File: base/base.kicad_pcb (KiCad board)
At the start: 2 copper layers, 51.4 x 20.5 mm, 12 parts, among them J1 Game Boy, J2 Game Gear, J3 Programming, U1 HC139, U2 PIC10F200-IOT

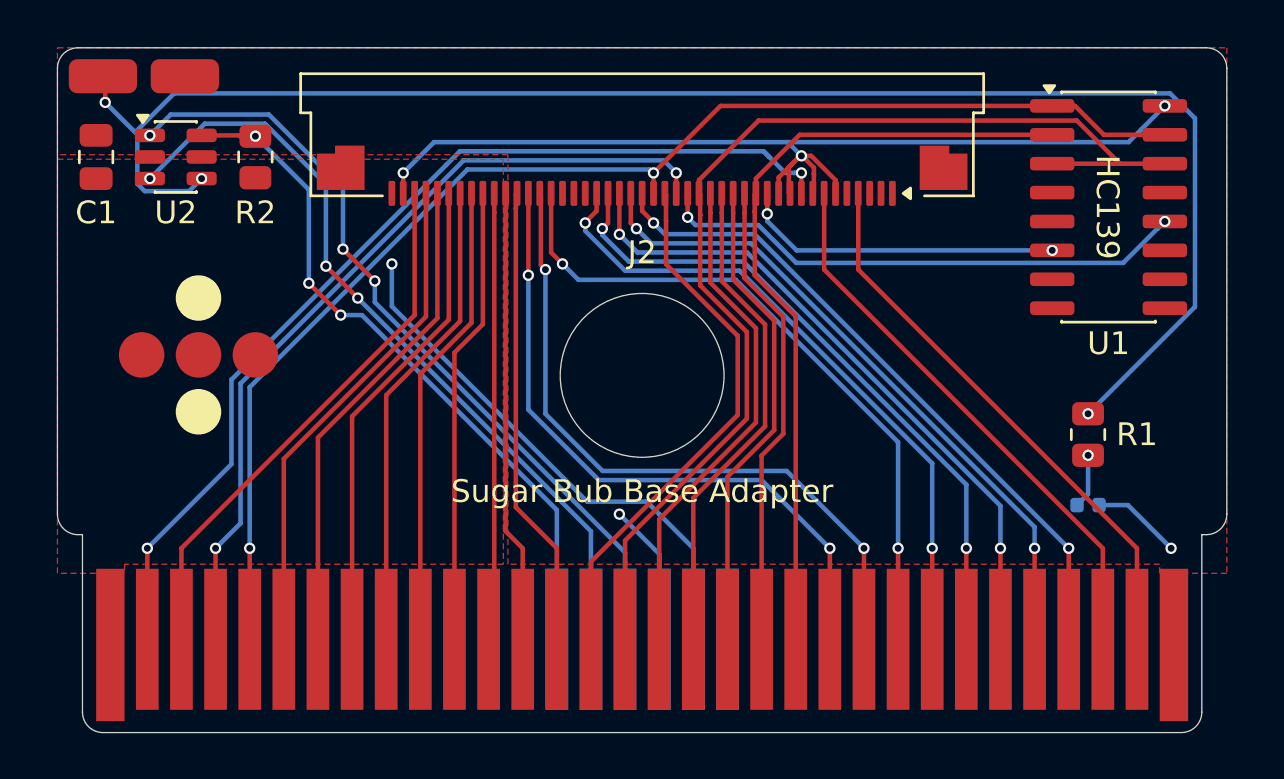
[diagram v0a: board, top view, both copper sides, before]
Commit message: Widen adapter board to 52.4mm
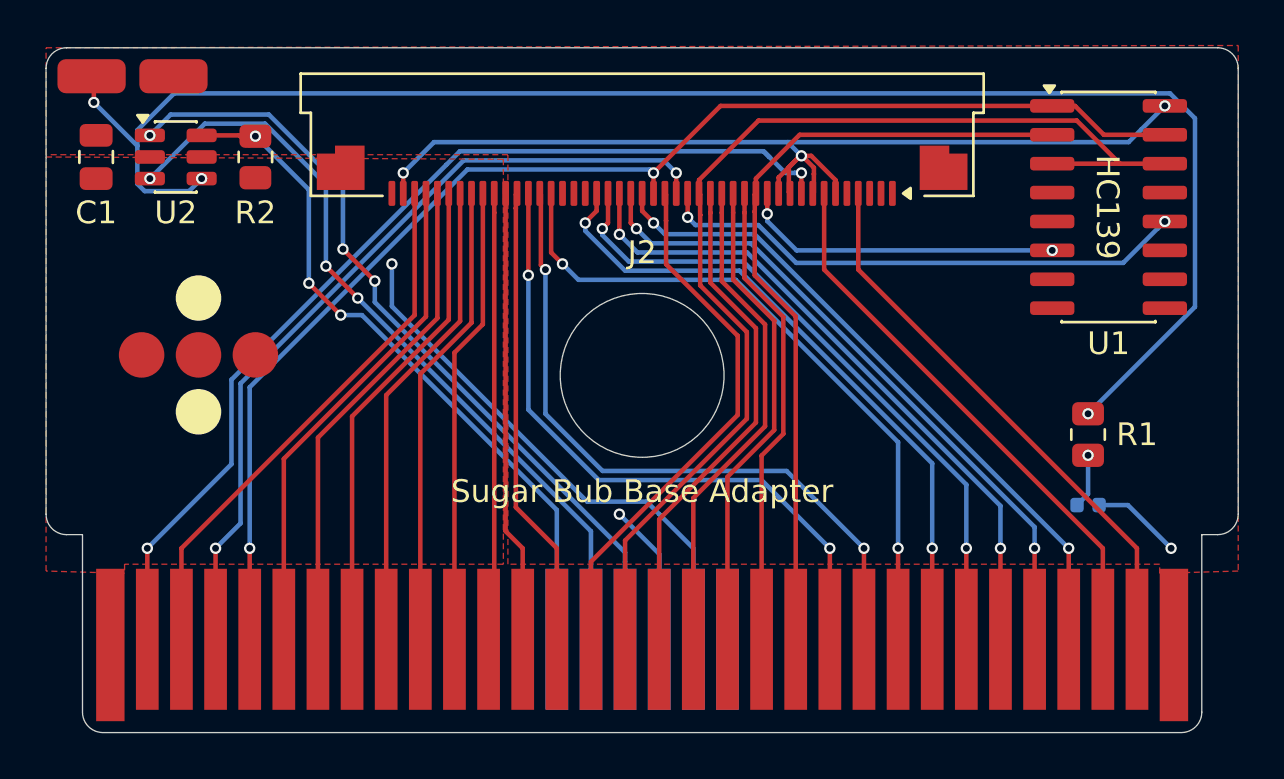
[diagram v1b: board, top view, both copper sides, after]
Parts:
- moved TP1 0.50 mm to (75.8, 79.2)
- moved TP2 0.50 mm to (79.4, 79.2)
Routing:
- net Net-(U2-GP2): track 71.1 -> 71.8 mm
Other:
- board size 51.4 x 20.5 mm -> 52.4 x 20.5 mm
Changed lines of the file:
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@@
 	(footprint "Connector_Wire:SolderWirePad_1x01_SMD_1.5x3mm"
 		(layer "F.Cu")
-		(at 79.9 79.25 90)
+		(at 79.4 79.25 90)
 		(descr "Wire Pad, Square, SMD Pad,  1.5mm x 3mm")
 		(tags "MeasurementPoint Square SMDPad 1.5mmx3mm ")
@@
 	(footprint "Connector_Wire:SolderWirePad_1x01_SMD_1.5x3mm"
 		(layer "F.Cu")
-		(at 76.3 79.25 90)
+		(at 75.8 79.25 90)
 		(descr "Wire Pad, Square, SMD Pad,  1.5mm x 3mm")
 		(tags "MeasurementPoint Square SMDPad 1.5mmx3mm ")
@@
 		(fp_line
 			(start -24.6 -4.6)
-			(end -24.8 -4.6)
+			(end -25.3 -4.6)
 			(stroke
 				(width 0.05)
@@
 		(fp_line
 			(start 24.6 -4.6)
-			(end 24.8 -4.6)
+			(end 25.3 -4.6)
 			(stroke
 				(width 0.05)
@@
 		)
 		(fp_arc
-			(start -24.8 -4.6)
-			(mid -25.436396 -4.863604)
-			(end -25.7 -5.5)
+			(start -25.3 -4.6)
+			(mid -25.936396 -4.863604)
+			(end -26.2 -5.5)
 			(stroke
 				(width 0.05)
@@
 		)
 		(fp_arc
-			(start 25.7 -5.5)
-			(mid 25.436396 -4.863604)
-			(end 24.8 -4.6)
+			(start 26.2 -5.5)
+			(mid 25.936396 -4.863604)
+			(end 25.3 -4.6)
 			(stroke
 				(width 0.05)
@@
 			(layer "F.CrtYd")
 		)
+		(fp_text user "${REFERENCE}"
+			(at 0 9.1 0)
+			(unlocked yes)
+			(layer "F.Fab")
+			(effects
+				(font
+					(size 1 1)
+					(thickness 0.15)
+				)
+			)
+		)
 		(pad "1" connect rect
 			(at -23.375 0.25)
@@
 	)
 	(gr_line
-		(start 124.8 78)
-		(end 75.2 78)
+		(start 125.3 78)
+		(end 74.7 78)
 		(stroke
 			(width 0.05)
@@
 	)
 	(gr_line
-		(start 125.7 98.5)
-		(end 125.7 78.9)
+		(start 126.2 98.5)
+		(end 126.2 78.9)
 		(stroke
 			(width 0.05)
@@
 	)
 	(gr_arc
-		(start 124.8 78)
-		(mid 125.436396 78.263604)
-		(end 125.7 78.9)
+		(start 125.3 78)
+		(mid 125.936396 78.263604)
+		(end 126.2 78.9)
 		(stroke
 			(width 0.05)
@@
 	)
 	(gr_arc
-		(start 74.3 78.9)
-		(mid 74.563604 78.263604)
-		(end 75.2 78)
+		(start 73.8 78.9)
+		(mid 74.063604 78.263604)
+		(end 74.7 78)
 		(stroke
 			(width 0.05)
@@
 	)
 	(gr_line
-		(start 74.3 98.5)
-		(end 74.3 78.9)
+		(start 73.8 98.5)
+		(end 73.8 78.9)
 		(stroke
 			(width 0.05)
@@
 		(layer "Dwgs.User")
 		(pts
-			(xy 75.3 78) (xy 76.2 108.1)
+			(xy 74.7 78) (xy 76.2 108.1)
 		)
 		(height -4.8)
@@
 		)
 		(gr_text "30.1"
-			(at 69.35 93.05 90)
+			(at 68.75 93.05 90)
 			(layer "Dwgs.User")
 			(effects
@@
 		(layer "Dwgs.User")
 		(pts
-			(xy 74.3 98.5) (xy 125.7 98.5)
+			(xy 73.8 98.5) (xy 126.2 98.5)
 		)
 		(height 18.5)
@@
 			(keep_text_aligned yes)
 		)
-		(gr_text "51.4"
+		(gr_text "52.4"
 			(at 100 115.85 0)
 			(layer "Dwgs.User")
@@
 	)
 	(segment
-		(start 76.4 80.4)
-		(end 76.4 79.35)
+		(start 75.9 80.4)
+		(end 75.9 79.35)
 		(width 0.2)
 		(layer "F.Cu")
@@
 	)
 	(via
-		(at 76.4 80.4)
+		(at 75.9 80.4)
 		(size 0.5)
 		(drill 0.3)
@@
 	)
 	(segment
+		(start 77.8115 81.8115)
+		(end 77.8115 82.3115)
+		(width 0.2)
+		(layer "B.Cu")
+		(net 50)
+	)
+	(segment
 		(start 79.429268 80.004)
 		(end 77.8115 81.621768)
@@
 	)
 	(segment
-		(start 77.8115 81.8115)
+		(start 77.8115 82.3115)
 		(end 77.8115 83.978232)
 		(width 0.2)
@@
 	)
 	(segment
-		(start 77.8115 83.978232)
-		(end 78.134268 84.301)
+		(start 75.9 80.4)
+		(end 77.8115 82.3115)
 		(width 0.2)
 		(layer "B.Cu")
@@
 	)
 	(segment
-		(start 124.3 89.3875)
-		(end 124.3 81.100768)
+		(start 77.8115 83.978232)
+		(end 78.134268 84.301)
 		(width 0.2)
 		(layer "B.Cu")
@@
 	)
 	(segment
-		(start 76.4 80.4)
-		(end 77.8115 81.8115)
+		(start 124.3 89.3875)
+		(end 124.3 81.100768)
 		(width 0.2)
 		(layer "B.Cu")
@@
 		(polygon
 			(pts
-				(xy 74.3 82.9) (xy 93.9 82.9) (xy 93.9 100.700606) (xy 77.25 100.7) (xy 77.25 101.1) (xy 74.3 101.1)
+				(xy 73.8 82.8) (xy 93.9 82.9) (xy 93.9 100.700606) (xy 77.25 100.7) (xy 77.25 101.1) (xy 73.8 101)
 			)
 		)
@@
 		(polygon
 			(pts
-				(xy 94.1 82.7) (xy 74.3 82.7) (xy 74.3 78) (xy 125.7 78) (xy 125.7 101.1) (xy 122.75 101.1) (xy 122.75 100.7)
+				(xy 94.1 82.7) (xy 73.8 82.7) (xy 73.8 78) (xy 126.2 77.9) (xy 126.2 101) (xy 122.75 101.1) (xy 122.75 100.7)
 				(xy 94.1 100.7)
 			)

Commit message: Add additional decoupling cap to base adapter
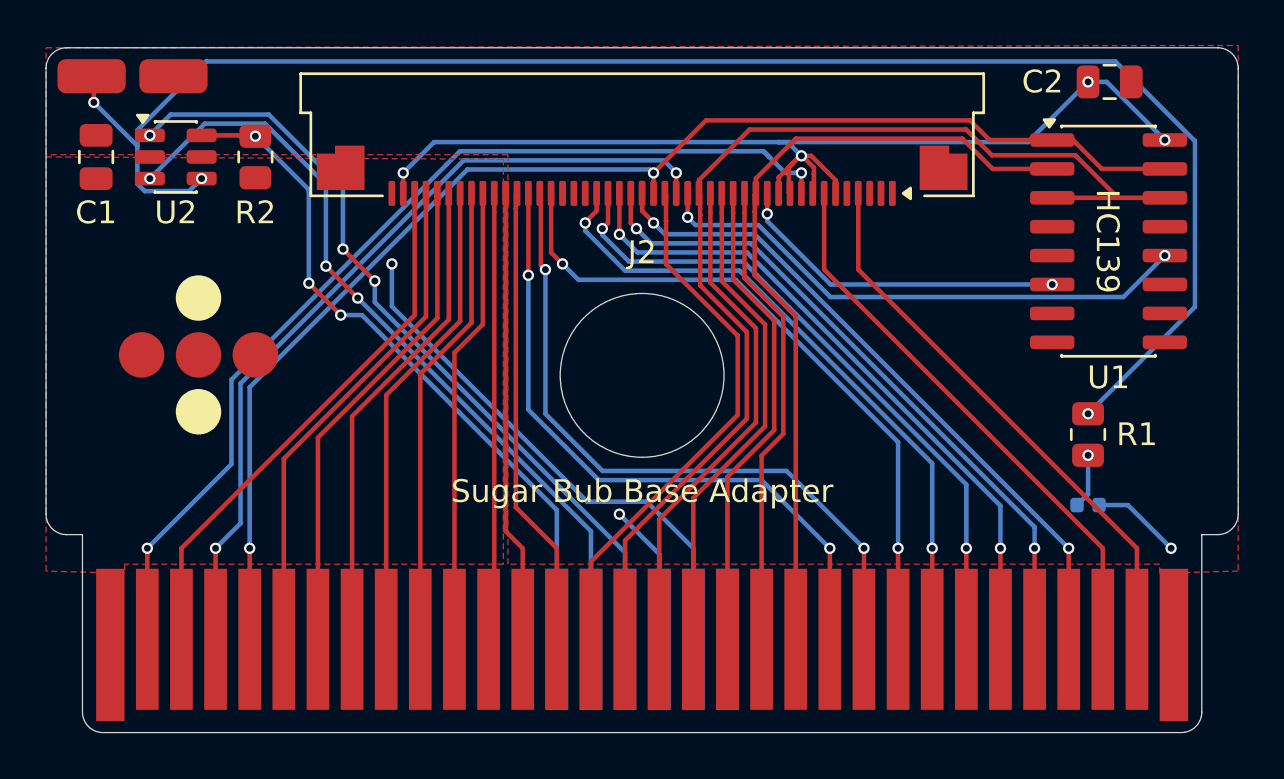
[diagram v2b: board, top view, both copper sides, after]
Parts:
- added C2: 0.1nF, Capacitor_SMD:C_0805_2012Metric, F.Cu at (120.5, 79.5)
- moved U1 1.50 mm to (120.5, 86.5)
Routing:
- net +5V: track 68.2 -> 70.1 mm, vias 4 -> 5
- net /M0-7: track 23.6 -> 24.2 mm
- net /M8-13: track 14.3 -> 14.9 mm
- net Net-(U2-GP2): track 71.8 -> 72.4 mm

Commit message: Add /Refresh to SMS and shrink logo
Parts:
- TP3: footprint SugarBub:SugarBub_Symbol -> SugarBub:SugarBub_Symbol_7mm
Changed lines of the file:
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@@
 		)
 	)
-	(footprint "SugarBub:SugarBub_Symbol"
+	(footprint "SugarBub:SugarBub_Symbol_7mm"
 		(layer "F.Cu")
 		(at 80.5 91.5)

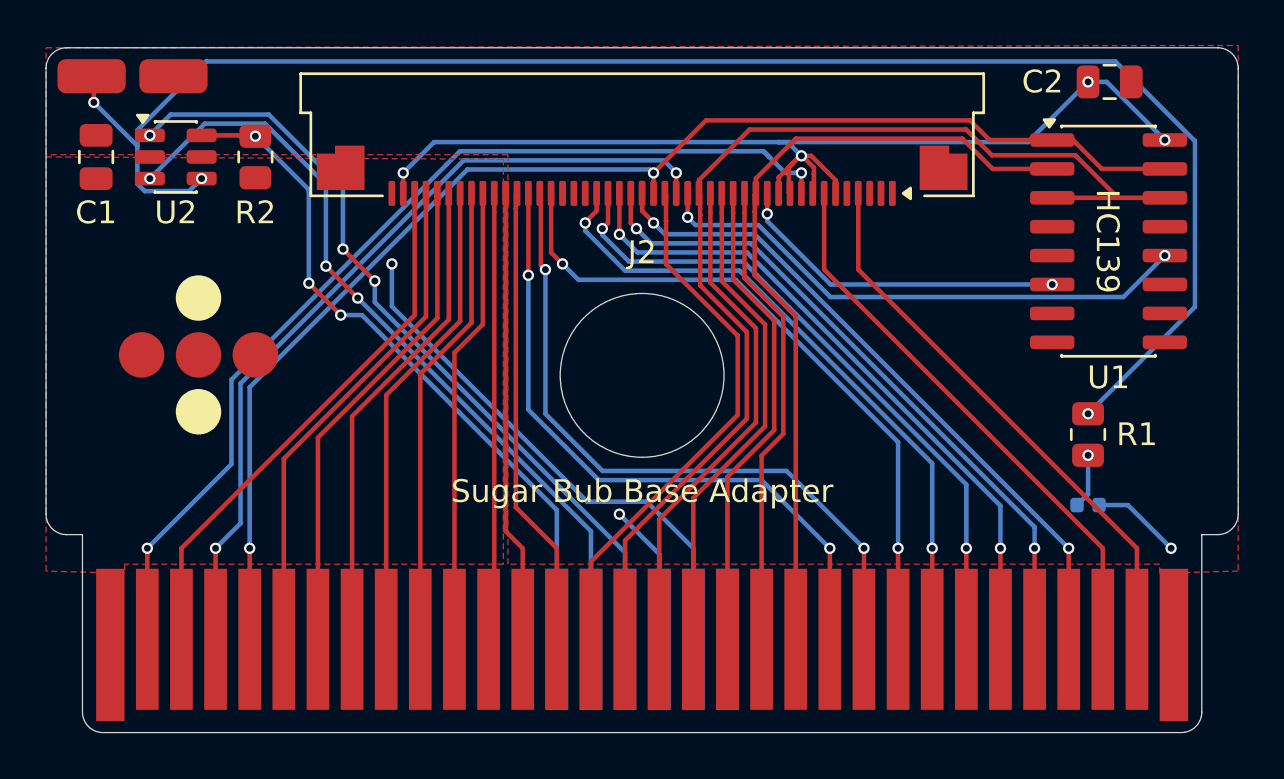
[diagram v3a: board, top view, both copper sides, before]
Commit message: Mark Analogue Pocket components as DNP
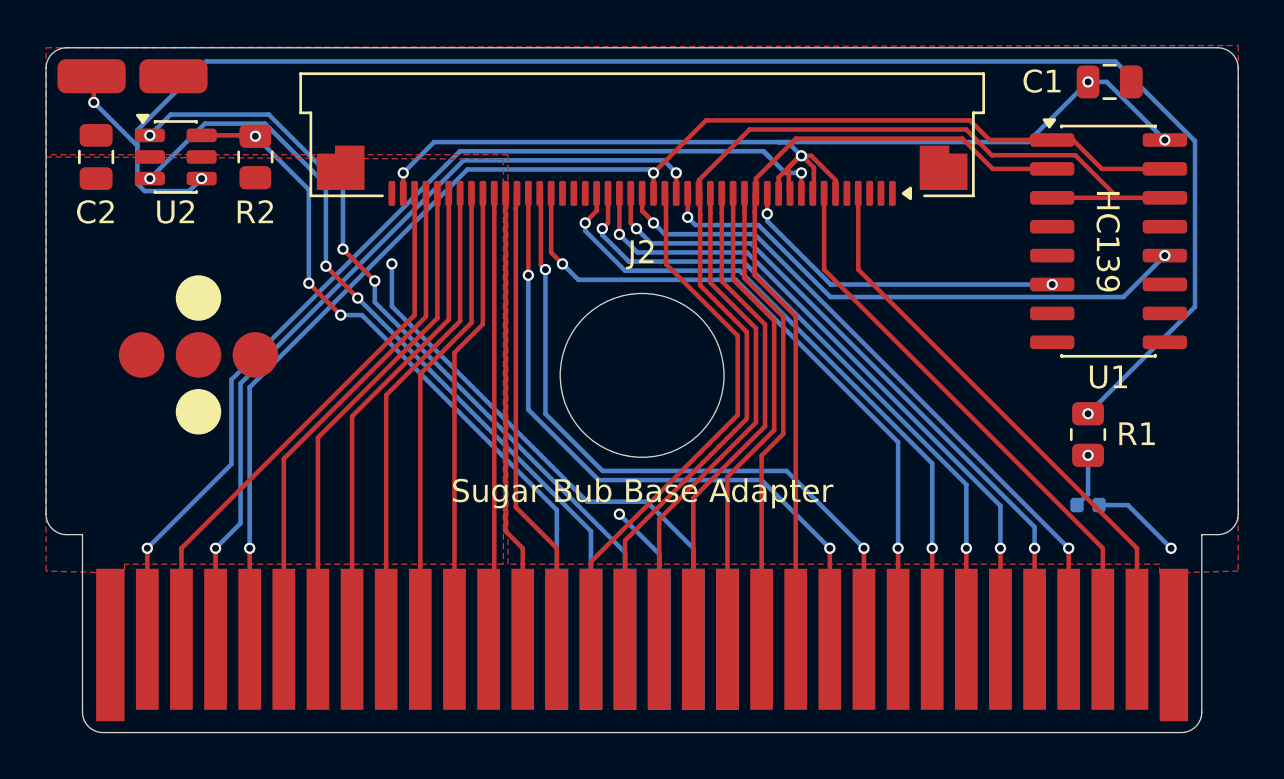
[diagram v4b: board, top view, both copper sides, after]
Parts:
- renumbered C2 to C1, C1 to C2
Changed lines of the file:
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@@
 		(descr "Capacitor SMD 0805 (2012 Metric), square (rectangular) end terminal, IPC-7351 nominal, (Body size source: IPC-SM-782 page 76, https://www.pcb-3d.com/wordpress/wp-content/uploads/ipc-sm-782a_amendment_1_and_2.pdf, https://docs.google.com/spreadsheets/d/1BsfQQcO9C6DZCsRaXUlFlo91Tg2WpOkGARC1WS5S8t0/edit?usp=sharing), generated with kicad-footprint-generator")
 		(tags "capacitor")
-		(property "Reference" "C2"
+		(property "Reference" "C1"
 			(at -2.95 0 0)
 			(layer "F.SilkS")
@@
 		(sheetname "/")
 		(sheetfile "base.kicad_sch")
-		(attr smd)
+		(attr smd dnp)
 		(fp_line
 			(start -0.91 -1.56)
@@
 		(sheetname "/")
 		(sheetfile "base.kicad_sch")
-		(attr smd)
+		(attr smd dnp)
 		(fp_line
 			(start -0.227064 0.735)
@@
 		(sheetname "/")
 		(sheetfile "base.kicad_sch")
-		(attr smd)
+		(attr smd dnp)
 		(fp_line
 			(start -0.227064 -0.735)
@@
 		(descr "Capacitor SMD 0805 (2012 Metric), square (rectangular) end terminal, IPC-7351 nominal, (Body size source: IPC-SM-782 page 76, https://www.pcb-3d.com/wordpress/wp-content/uploads/ipc-sm-782a_amendment_1_and_2.pdf, https://docs.google.com/spreadsheets/d/1BsfQQcO9C6DZCsRaXUlFlo91Tg2WpOkGARC1WS5S8t0/edit?usp=sharing), generated with kicad-footprint-generator")
 		(tags "capacitor")
-		(property "Reference" "C1"
+		(property "Reference" "C2"
 			(at -2.45 0 180)
 			(layer "F.SilkS")
@@
 		(sheetname "/")
 		(sheetfile "base.kicad_sch")
-		(attr smd)
+		(attr smd dnp)
 		(fp_line
 			(start -0.261252 -0.735)
@@
 		(sheetname "/")
 		(sheetfile "base.kicad_sch")
-		(attr smd)
+		(attr smd dnp)
 		(fp_circle
 			(center -1.09 0)
